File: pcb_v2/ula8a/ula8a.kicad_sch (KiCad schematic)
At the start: 21 parts, among them J1 designador, J2 acc, J3 adder, J4 xor, J5 bitwise, J6 shifter, J7 sx, U1 74LS86, U2 74LS86, U3 74LS86, U4 74LS86, U5 74LS244, U6 74LS86, U7 74LS86

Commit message: roteamento refeito; ainda pendente
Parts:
- removed J2: acc, edge_connector:edge-conector-14, symbol Connector_Generic:Conn_02x14_Top_Bottom
- added C10, C11, C12, C13, C14, C15, C17, C21, C22, C8, C9: 100nF, Capacitor_THT:C_Disc_D5.1mm_W3.2mm_P5.00mm, symbol Device:C
- added D1, D2, D3, D4, D5, D6, D7, D8: 1N4148, Diode_THT:D_DO-35_SOD27_P7.62mm_Horizontal, symbol Diode:1N4148
- added D10: ULA, LED_THT:LED_D5.0mm, symbol Device:LED
- added D11: ~{LOWER}, LED_THT:LED_D5.0mm, symbol Device:LED
- added D12: ~{ULA}, LED_THT:LED_D5.0mm, symbol Device:LED
- added D13: ~{UPPER}, LED_THT:LED_D5.0mm, symbol Device:LED
- added D14: INT, LED_THT:LED_D5.0mm, symbol Device:LED
- added D15: NEG, LED_THT:LED_D5.0mm, symbol Device:LED
- added D16: OVF, LED_THT:LED_D5.0mm, symbol Device:LED
- added D17: CARRY, LED_THT:LED_D5.0mm, symbol Device:LED
- added D18: ZERO, LED_THT:LED_D5.0mm, symbol Device:LED
- added D19: WPSW, LED_THT:LED_D5.0mm, symbol Device:LED
- added D20: WACC, LED_THT:LED_D5.0mm, symbol Device:LED
- added D9: POWER, LED_THT:LED_D5.0mm, symbol Device:LED
- added J7: ula_opp, edge_connector:male-edge-connector-44, symbol Connector_Generic:Conn_02x22_Top_Bottom
- added J8: bus_mgrf_1, Connector_PinHeader_2.54mm:PinHeader_2x08_P2.54mm_Vertical, symbol Connector_Generic:Conn_02x08_Odd_Even
- added J9: bus_mgrf_2, Connector_PinHeader_2.54mm:PinHeader_2x08_P2.54mm_Vertical, symbol Connector_Generic:Conn_02x08_Odd_Even
- added Q1: BC548, Package_TO_SOT_THT:TO-92_Inline, symbol Transistor_BJT:BC548
- added R1, R2: 10K, Resistor_THT:R_Axial_DIN0207_L6.3mm_D2.5mm_P7.62mm_Horizontal, symbol Device:R
- added R10, R11, R12, R13, R14, R15, R16, R17, R18, R19, R20, R9: 1K, Resistor_THT:R_Axial_DIN0207_L6.3mm_D2.5mm_P7.62mm_Horizontal, symbol Device:R
- added U10, U12, U17, U21: 74LS244, Package_DIP:DIP-20_W7.62mm, symbol 74xx:74LS244
- added U11: 74LS86, Package_DIP:DIP-14_W7.62mm, symbol 74xx:74LS86
- added U13, U8: 74LS574, Package_DIP:DIP-20_W7.62mm, symbol 74xx:74LS574
- added U14, U9: 74LS00, Package_DIP:DIP-14_W7.62mm, symbol 74xx:74LS00
- added U15: MC14495P, Package_DIP:DIP-16_W7.62mm, symbol Driver_LED:MC14495P
- added U16: SA39-11EWA, Display_7Segment:Sx39-1xxxxx, symbol Display_Character:SA39-11EWA
- added U22: 74LS04, Package_DIP:DIP-14_W7.62mm, symbol 74xx:74LS04
- C1, C2, C3, C4, C5, C6, C7: footprint (none) -> Capacitor_THT:C_Disc_D5.1mm_W3.2mm_P5.00mm
- J1: footprint edge_connector:edge-connector-44 -> edge_connector:male-edge-connector-44
- J2: renamed from J3; value adder -> ula_opp; footprint edge_connector:edge-connector-44 -> edge_connector:male-edge-connector-44
- J3: renamed from J4; value xor -> ula_opp; footprint edge_connector:edge-connector-44 -> edge_connector:male-edge-connector-44
- J4: renamed from J5; value bitwise -> ula_opp; footprint edge_connector:edge-connector-44 -> edge_connector:male-edge-connector-44
- J5: renamed from J6; value shifter -> ula_opp; footprint edge_connector:edge-connector-44 -> edge_connector:male-edge-connector-44
- J6: renamed from J7; value sx -> ula_opp; footprint edge_connector:edge-connector-44 -> edge_connector:male-edge-connector-44
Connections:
- net carry_in is gone; now on net +5V: J2.23 (Pin_23), J3.23 (Pin_23), J4.23 (Pin_23), J5.23 (Pin_23), J6.23 (Pin_23)
- net clrif is gone; now on net ~{select_sx}: J1.28 (Pin_28)
- net data_out_0 is gone; now on net data_0: U5.18 (O0a)
- net data_out_1 is gone; now on net data_1: U5.16 (O1a)
- net data_out_2 is gone; now on net data_2: U5.14 (O2a)
- net data_out_3 is gone; now on net data_3: U5.12 (O3a)
- net data_out_4 is gone; now on net data_4: U5.9 (O0b)
- net data_out_5 is gone; now on net data_5: U5.7 (O1b)
- net data_out_6 is gone; now on net data_6: U5.5 (O2b)
- net data_out_7 is gone; now on net data_7: U5.3 (O3b)
- net setif is gone; now on net invert_upper_bus: J1.6 (Pin_6)
- net +5V: now also J1.1 (Pin_1), J1.23 (Pin_23), J2.1 (Pin_1), J3.1 (Pin_1), J4.1 (Pin_1), J5.1 (Pin_1), J6.1 (Pin_1), C10.2, C11.2, C12.2, C13.2, C14.2, C15.2, C17.2, C21.2, C22.2, C8.2, C9.2, J7.1 (Pin_1), J7.23 (Pin_23), J8.1 (Pin_1), J8.2 (Pin_2), R9.1, U10.20 (VCC), U11.12, U11.14 (VCC), U11.9, U12.20 (VCC), U13.20 (VCC), U14.1, U14.14 (VCC), U14.2, U15.16 (VCC), U17.20 (VCC), U21.20 (VCC), U22.11, U22.13, U22.14 (VCC), U8.20 (VCC), U9.12, U9.13, U9.14 (VCC); no longer J1.14 (Pin_14), J1.36 (Pin_36), J2.10 (Pin_10), J2.32 (Pin_32), J3.10 (Pin_10), J3.32 (Pin_32), J4.10 (Pin_10), J4.32 (Pin_32), J5.10 (Pin_10), J5.32 (Pin_32), J6.10 (Pin_10), J6.32 (Pin_32)
- net GND: now also J1.22 (Pin_22), J1.44 (Pin_44), J2.22 (Pin_22), J2.44 (Pin_44), J3.22 (Pin_22), J3.44 (Pin_44), J4.22 (Pin_22), J4.44 (Pin_44), J5.22 (Pin_22), J5.44 (Pin_44), J6.22 (Pin_22), J6.44 (Pin_44), C10.1, C11.1, C12.1, C13.1, C14.1, C15.1, C17.1, C21.1, C22.1, C8.1, C9.1, D9.1 (K), J7.22 (Pin_22), J7.44 (Pin_44), J8.15 (Pin_15), J8.16 (Pin_16), Q1.3 (E), R1.2, R10.2, R11.2, R12.2, R13.2, R14.2, R15.2, R16.2, R17.2, R18.2, R19.2, R20.2, U10.10 (GND), U11.7 (GND), U12.10 (GND), U12.13 (I1b), U12.15 (I2b), U12.17 (I3b), U13.1 (OE), U13.10 (GND), U13.6 (D4), U13.7 (D5), U13.8 (D6), U13.9 (D7), U14.7 (GND), U15.7 (~{CLK}), U15.8 (GND), U17.10 (GND), U17.11 (I0b), U17.13 (I1b), U17.15 (I2b), U17.17 (I3b), U21.10 (GND), U21.11 (I0b), U21.13 (I1b), U21.15 (I2b), U21.17 (I3b), U22.7 (GND), U8.1 (OE), U8.10 (GND), U9.7 (GND); no longer J1.15 (Pin_15), J1.37 (Pin_37), J2.11 (Pin_11), J2.33 (Pin_33), J3.11 (Pin_11), J3.33 (Pin_33), J4.11 (Pin_11), J4.33 (Pin_33), J5.11 (Pin_11), J5.33 (Pin_33), J6.11 (Pin_11), J6.33 (Pin_33)
- net invert_lower_bus: now also J1.2 (Pin_2), D11.2 (A); no longer J1.1 (Pin_1)
- net invert_ula_bus: now also J1.5 (Pin_5), D12.2 (A); no longer J1.4 (Pin_4)
- net invert_upper_bus: now also D13.2 (A); no longer J1.5 (Pin_5)
- net lower_bus0: now also J2.2 (Pin_2), J3.2 (Pin_2), J4.2 (Pin_2), J5.2 (Pin_2), J6.2 (Pin_2), J7.2 (Pin_2); no longer J2.1 (Pin_1), J3.1 (Pin_1), J4.1 (Pin_1), J5.1 (Pin_1), J6.1 (Pin_1)
- net lower_bus1: now also J2.3 (Pin_3), J3.3 (Pin_3), J4.3 (Pin_3), J5.3 (Pin_3), J6.3 (Pin_3), J7.3 (Pin_3); no longer J2.2 (Pin_2), J3.2 (Pin_2), J4.2 (Pin_2), J5.2 (Pin_2), J6.2 (Pin_2)
- net lower_bus2: now also J2.4 (Pin_4), J3.4 (Pin_4), J4.4 (Pin_4), J5.4 (Pin_4), J6.4 (Pin_4), J7.4 (Pin_4); no longer J2.3 (Pin_3), J3.3 (Pin_3), J4.3 (Pin_3), J5.3 (Pin_3), J6.3 (Pin_3)
- net lower_bus3: now also J2.5 (Pin_5), J3.5 (Pin_5), J4.5 (Pin_5), J5.5 (Pin_5), J6.5 (Pin_5), J7.5 (Pin_5); no longer J2.4 (Pin_4), J3.4 (Pin_4), J4.4 (Pin_4), J5.4 (Pin_4), J6.4 (Pin_4)
- net lower_bus4: now also J2.6 (Pin_6), J3.6 (Pin_6), J4.6 (Pin_6), J5.6 (Pin_6), J6.6 (Pin_6), J7.6 (Pin_6); no longer J2.5 (Pin_5), J3.5 (Pin_5), J4.5 (Pin_5), J5.5 (Pin_5), J6.5 (Pin_5)
- net lower_bus5: now also J2.7 (Pin_7), J3.7 (Pin_7), J4.7 (Pin_7), J5.7 (Pin_7), J6.7 (Pin_7), J7.7 (Pin_7); no longer J2.6 (Pin_6), J3.6 (Pin_6), J4.6 (Pin_6), J5.6 (Pin_6), J6.6 (Pin_6)
- net lower_bus6: now also J2.8 (Pin_8), J3.8 (Pin_8), J4.8 (Pin_8), J5.8 (Pin_8), J6.8 (Pin_8), J7.8 (Pin_8); no longer J2.7 (Pin_7), J3.7 (Pin_7), J4.7 (Pin_7), J5.7 (Pin_7), J6.7 (Pin_7)
- net lower_bus7: now also J2.9 (Pin_9), J3.9 (Pin_9), J4.9 (Pin_9), J5.9 (Pin_9), J6.9 (Pin_9), J7.9 (Pin_9), U11.1; no longer J2.8 (Pin_8), J3.8 (Pin_8), J4.8 (Pin_8), J5.8 (Pin_8), J6.8 (Pin_8)
- net rd_addr_0: now also J1.19 (Pin_19), J9.8 (Pin_8); no longer J1.20 (Pin_20)
- net rd_addr_1: now also J1.20 (Pin_20), J9.10 (Pin_10); no longer J1.21 (Pin_21)
- net rd_addr_2: now also J1.40 (Pin_40), J9.12 (Pin_12); no longer J1.41 (Pin_41)
- net rd_addr_3: now also J1.41 (Pin_41), J9.14 (Pin_14); no longer J1.42 (Pin_42)
- net rd_addr_4: now also J1.42 (Pin_42), J9.16 (Pin_16); no longer J1.43 (Pin_43)
- net to_acc_0: now also D1.2 (A), U8.2 (D0)
- net to_acc_1: now also D2.2 (A), U8.3 (D1)
- net to_acc_2: now also D3.2 (A), U8.4 (D2)
- net to_acc_3: now also D4.2 (A), U8.5 (D3)
- net to_acc_4: now also D5.2 (A), U8.6 (D4)
- net to_acc_5: now also D6.2 (A), U8.7 (D5)
- net to_acc_6: now also D7.2 (A), U8.8 (D6)
- net to_acc_7: now also D8.2 (A), U11.4, U17.8 (I3a), U8.9 (D7)
- net ula_bus0: now also J2.36 (Pin_36), J3.36 (Pin_36), J4.36 (Pin_36), J5.36 (Pin_36), J6.36 (Pin_36), J7.36 (Pin_36), U10.18 (O0a); no longer J2.37 (Pin_37), J3.37 (Pin_37), J4.37 (Pin_37), J5.37 (Pin_37), J6.37 (Pin_37)
- net ula_bus1: now also J2.37 (Pin_37), J3.37 (Pin_37), J4.37 (Pin_37), J5.37 (Pin_37), J6.37 (Pin_37), J7.37 (Pin_37), U10.16 (O1a); no longer J2.38 (Pin_38), J3.38 (Pin_38), J4.38 (Pin_38), J5.38 (Pin_38), J6.38 (Pin_38)
- net ula_bus2: now also J2.38 (Pin_38), J3.38 (Pin_38), J4.38 (Pin_38), J5.38 (Pin_38), J6.38 (Pin_38), J7.38 (Pin_38), U10.14 (O2a); no longer J2.39 (Pin_39), J3.39 (Pin_39), J4.39 (Pin_39), J5.39 (Pin_39), J6.39 (Pin_39)
- net ula_bus3: now also J2.39 (Pin_39), J3.39 (Pin_39), J4.39 (Pin_39), J5.39 (Pin_39), J6.39 (Pin_39), J7.39 (Pin_39), U10.12 (O3a); no longer J2.40 (Pin_40), J3.40 (Pin_40), J4.40 (Pin_40), J5.40 (Pin_40), J6.40 (Pin_40)
- net ula_bus4: now also J2.40 (Pin_40), J3.40 (Pin_40), J4.40 (Pin_40), J5.40 (Pin_40), J6.40 (Pin_40), J7.40 (Pin_40), U10.9 (O0b); no longer J2.41 (Pin_41), J3.41 (Pin_41), J4.41 (Pin_41), J5.41 (Pin_41), J6.41 (Pin_41)
- net ula_bus5: now also J2.41 (Pin_41), J3.41 (Pin_41), J4.41 (Pin_41), J5.41 (Pin_41), J6.41 (Pin_41), J7.41 (Pin_41), U10.7 (O1b); no longer J2.42 (Pin_42), J3.42 (Pin_42), J4.42 (Pin_42), J5.42 (Pin_42), J6.42 (Pin_42)
- net ula_bus6: now also J2.42 (Pin_42), J3.42 (Pin_42), J4.42 (Pin_42), J5.42 (Pin_42), J6.42 (Pin_42), J7.42 (Pin_42), U10.5 (O2b); no longer J2.43 (Pin_43), J3.43 (Pin_43), J4.43 (Pin_43), J5.43 (Pin_43), J6.43 (Pin_43)
- net ula_bus7: now also J2.43 (Pin_43), J3.43 (Pin_43), J4.43 (Pin_43), J5.43 (Pin_43), J6.43 (Pin_43), J7.43 (Pin_43), U10.3 (O3b); no longer J2.44 (Pin_44), J3.44 (Pin_44), J4.44 (Pin_44), J5.44 (Pin_44), J6.44 (Pin_44)
- net ula_enable: now also J1.33 (Pin_33), D10.2 (A), J9.2 (Pin_2), R2.2, U22.1, U9.2; no longer J1.32 (Pin_32)
- net upper_bus0: now also J2.25 (Pin_25), J3.25 (Pin_25), J4.25 (Pin_25), J5.25 (Pin_25), J6.25 (Pin_25), J7.25 (Pin_25); no longer J2.24 (Pin_24), J3.24 (Pin_24), J4.24 (Pin_24), J5.24 (Pin_24), J6.24 (Pin_24)
- net upper_bus1: now also J2.26 (Pin_26), J3.26 (Pin_26), J4.26 (Pin_26), J5.26 (Pin_26), J6.26 (Pin_26), J7.26 (Pin_26); no longer J2.25 (Pin_25), J3.25 (Pin_25), J4.25 (Pin_25), J5.25 (Pin_25), J6.25 (Pin_25)
- net upper_bus2: now also J2.27 (Pin_27), J3.27 (Pin_27), J4.27 (Pin_27), J5.27 (Pin_27), J6.27 (Pin_27), J7.27 (Pin_27); no longer J2.26 (Pin_26), J3.26 (Pin_26), J4.26 (Pin_26), J5.26 (Pin_26), J6.26 (Pin_26)
- net upper_bus3: now also J2.28 (Pin_28), J3.28 (Pin_28), J4.28 (Pin_28), J5.28 (Pin_28), J6.28 (Pin_28), J7.28 (Pin_28); no longer J2.27 (Pin_27), J3.27 (Pin_27), J4.27 (Pin_27), J5.27 (Pin_27), J6.27 (Pin_27)
- net upper_bus4: now also J2.29 (Pin_29), J3.29 (Pin_29), J4.29 (Pin_29), J5.29 (Pin_29), J6.29 (Pin_29), J7.29 (Pin_29); no longer J2.28 (Pin_28), J3.28 (Pin_28), J4.28 (Pin_28), J5.28 (Pin_28), J6.28 (Pin_28)
- net upper_bus5: now also J2.30 (Pin_30), J3.30 (Pin_30), J4.30 (Pin_30), J5.30 (Pin_30), J6.30 (Pin_30), J7.30 (Pin_30); no longer J2.29 (Pin_29), J3.29 (Pin_29), J4.29 (Pin_29), J5.29 (Pin_29), J6.29 (Pin_29)
- net upper_bus6: now also J2.31 (Pin_31), J3.31 (Pin_31), J4.31 (Pin_31), J5.31 (Pin_31), J6.31 (Pin_31), J7.31 (Pin_31); no longer J2.30 (Pin_30), J3.30 (Pin_30), J4.30 (Pin_30), J5.30 (Pin_30), J6.30 (Pin_30)
- net upper_bus7: now also J2.32 (Pin_32), J3.32 (Pin_32), J4.32 (Pin_32), J5.32 (Pin_32), J6.32 (Pin_32), J7.32 (Pin_32), U11.2; no longer J2.31 (Pin_31), J3.31 (Pin_31), J4.31 (Pin_31), J5.31 (Pin_31), J6.31 (Pin_31)
- net wr_addr_0: now also J1.30 (Pin_30), J9.5 (Pin_5), U15.5 (A); no longer J1.29 (Pin_29)
- net wr_addr_1: now also J1.31 (Pin_31), J9.7 (Pin_7), U15.6 (B); no longer J1.30 (Pin_30)
- net wr_addr_2: now also J1.32 (Pin_32), J9.9 (Pin_9), U15.9 (C); no longer J1.31 (Pin_31)
- net wr_addr_3: now also J9.11 (Pin_11), U15.10 (D)
- net wr_addr_4: now also J9.13 (Pin_13)
- net write_acc: now also D20.2 (A), U22.9, U9.5
- net write_psw: now also D19.2 (A), U14.5, U22.3
- net ~{read_acc}: now also J1.21 (Pin_21); no longer J1.22 (Pin_22)
- net ~{read_psw}: now also J1.43 (Pin_43), U12.1 (OEa), U12.19 (OEb); no longer J1.44 (Pin_44)
- net ~{select_adder}: now also J1.26 (Pin_26), J3.15 (Pin_15), J4.15 (Pin_15), J5.15 (Pin_15), J6.15 (Pin_15), J7.15 (Pin_15); no longer J1.25 (Pin_25)
- net ~{select_bitwise}: now also J1.24 (Pin_24), J2.18 (Pin_18), J3.18 (Pin_18), J4.18 (Pin_18), J5.18 (Pin_18), J6.18 (Pin_18), J7.18 (Pin_18); no longer J1.23 (Pin_23), J4.15 (Pin_15)
- net ~{select_shifter}: now also J1.27 (Pin_27), J2.17 (Pin_17), J3.17 (Pin_17), J4.17 (Pin_17), J5.17 (Pin_17), J6.17 (Pin_17), J7.17 (Pin_17); no longer J1.26 (Pin_26), J5.15 (Pin_15)
- net ~{select_sx}: now also J2.19 (Pin_19), J3.19 (Pin_19), J4.19 (Pin_19), J5.19 (Pin_19), J6.19 (Pin_19), J7.19 (Pin_19); no longer J1.27 (Pin_27), J6.15 (Pin_15)
- net ~{select_xor}: now also J1.25 (Pin_25), J2.16 (Pin_16), J3.16 (Pin_16), J4.16 (Pin_16), J5.16 (Pin_16), J6.16 (Pin_16), J7.16 (Pin_16); no longer J1.24 (Pin_24), J3.15 (Pin_15)
- net at U5.2 (I0a), U6.2: now also U8.19 (Q0)
- net right/mode: now reaches J6.13 (Pin_13)
- net right/mode: now also J1.4 (Pin_4), J2.13 (Pin_13), J3.13 (Pin_13), J4.13 (Pin_13), J5.13 (Pin_13), J7.13 (Pin_13)
- net rotate/value: now reaches J6.14 (Pin_14)
- net rotate/value: now also J1.3 (Pin_3), J2.14 (Pin_14), J3.14 (Pin_14), J4.14 (Pin_14), J5.14 (Pin_14), J7.14 (Pin_14)
- net ~{select_cf}: now reaches J6.20 (Pin_20)
- net ~{select_cf}: now also J1.29 (Pin_29), J2.20 (Pin_20), J3.20 (Pin_20), J4.20 (Pin_20), J5.20 (Pin_20), J7.20 (Pin_20)
- net at U5.13 (I1b), U7.5: now also U8.14 (Q5)
- net at U5.11 (I0b), U7.2: now also U8.15 (Q4)
- net at U5.15 (I2b), U7.10: now also U8.13 (Q6)
- net at U5.17 (I3b), U7.13: now also U8.12 (Q7)
- net at U5.4 (I1a), U6.5: now also U8.18 (Q1)
- net at U5.6 (I2a), U6.10: now also U8.17 (Q2)
- net at U5.8 (I3a), U6.13: now also U8.16 (Q3)
- net carry_out renamed carry_flag_in
- net carry_flag_in: now also J7.35 (Pin_35), U11.5, U17.4 (I1a)
- net data_in_0 renamed data_0
- net data_0: now also J8.14 (Pin_14), U10.2 (I0a), U12.18 (O0a), U21.2 (I0a)
- net data_in_1 renamed data_1
- net data_1: now also J8.13 (Pin_13), U10.4 (I1a), U12.16 (O1a), U21.4 (I1a)
- net data_in_2 renamed data_2
- net data_2: now also J8.11 (Pin_11), U10.6 (I2a), U12.14 (O2a), U21.6 (I2a)
- net data_in_3 renamed data_3
- net data_3: now also J8.9 (Pin_9), U10.8 (I3a), U12.12 (O3a), U21.8 (I3a)
- net data_in_4 renamed data_4
- net data_4: now also J8.7 (Pin_7), U10.11 (I0b), U12.9 (O0b)
- net data_in_5 renamed data_5
- net data_5: now also J8.5 (Pin_5), U10.13 (I1b), U12.7 (O1b)
- net data_in_6 renamed data_6
- net data_6: now also J8.3 (Pin_3), U10.15 (I2b), U12.5 (O2b)
- net data_in_7 renamed data_7
- net data_7: now also J8.4 (Pin_4), U10.17 (I3b), U12.3 (O3b)
- removed net right/set: J1.3 (Pin_3), J5.16 (Pin_16), J6.16 (Pin_16)
- removed net rotate/clear: J1.2 (Pin_2), J5.17 (Pin_17), J6.17 (Pin_17)
- net write_clock renamed write_enable
- net write_enable: now also J9.15 (Pin_15)
- new net: D16.1 (K), R16.1
- new net: D1.1 (K), D2.1 (K), D3.1 (K), D4.1 (K), D5.1 (K), D6.1 (K), D7.1 (K), D8.1 (K), R1.1, U22.5
- new net: D18.1 (K), R18.1
- new net: U14.10, U9.3, U9.9
- new net: U17.1 (OEa), U17.19 (OEb), U22.2
- new net: D10.1 (K), R10.1
- new net: U11.10, U11.3
- new net: U10.1 (OEa), U10.19 (OEb), U22.8
- new net: U9.10, U9.6
- new net: U14.6, U14.9
- new net: U21.1 (OEa), U21.19 (OEb), U22.4
- new net: U13.5 (D3), U17.12 (O3a), U21.12 (O3a)
- new net: U13.4 (D2), U17.14 (O2a), U21.14 (O2a)
- new net: U13.3 (D1), U17.16 (O1a), U21.16 (O1a)
- new net: U13.2 (D0), U17.18 (O0a), U21.18 (O0a)
- new net: Q1.2 (B), R2.1
- new net: U11.6, U14.13
- new net: U15.3 (g), U16.1 (G)
- new net: U15.12 (a), U16.10 (A)
- new net: U15.2 (f), U16.2 (F)
- new net: Q1.1 (C), U16.3 (CA), U16.8 (CA)
- new net: U15.1 (e), U16.4 (E)
- new net: U15.15 (d), U16.5 (D)
- new net: U15.14 (c), U16.7 (C)
- new net: U15.13 (b), U16.9 (B)
- new net: U11.13, U14.11
- new net: U11.8, U14.12
- new net: D15.1 (K), R15.1
- new net: D19.1 (K), R19.1
- new net: D12.1 (K), R12.1
- new net: D17.1 (K), R17.1
- new net: D9.2 (A), R9.2
- new net: D13.1 (K), R13.1
- new net: D14.1 (K), R14.1
- new net: D11.1 (K), R11.1
- new net: D20.1 (K), R20.1
- new net carry_flag_out: D17.2 (A), J2.24 (Pin_24), J3.24 (Pin_24), J4.24 (Pin_24), J5.24 (Pin_24), J6.24 (Pin_24), J7.24 (Pin_24), J8.8 (Pin_8), U12.4 (I1a), U13.18 (Q1)
- new net clock: J9.4 (Pin_4), U14.4, U9.1, U9.4
- new net int_mask_in: D14.2 (A), J9.1 (Pin_1), U12.11 (I0b)
- new net load_ula_acc: U8.11 (Cp), U9.8
- new net load_ula_psw: U13.11 (Cp), U14.8
- new net negative_flag_out: D15.2 (A), J8.12 (Pin_12), U12.8 (I3a), U13.16 (Q3)
- new net overflow_flag_in: U11.11, U17.6 (I2a)
- new net overflow_flag_out: D16.2 (A), J8.10 (Pin_10), U12.6 (I2a), U13.17 (Q2)
- new net zero_flag_in: U17.2 (I0a), U22.6
- new net zero_flag_out: D18.2 (A), J8.6 (Pin_6), U12.2 (I0a), U13.19 (Q0)
- no-connect marks 79 -> 70
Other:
- moved on the sheet: C1, C2, C3, C4, C5, C6, C7, U1A, U1B, U1C, U1D, U1E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

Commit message: concluidas as modificações de layout na pcb
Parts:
- U16: footprint Display_7Segment:Sx39-1xxxxx -> 7segdisplay:1-digit-13mm
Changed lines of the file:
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@@
 			)
 		)
-		(property "Footprint" "Display_7Segment:Sx39-1xxxxx"
+		(property "Footprint" "7segdisplay:1-digit-13mm"
 			(at 123.19 262.89 0)
 			(effects

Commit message: .
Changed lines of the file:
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@@
 	)
 	(global_label "rd_addr_0"
-		(shape input)
+		(shape output)
 		(at 43.18 172.72 0)
 		(fields_autoplaced yes)
@@
 		)
 		(property "Intersheetrefs" "${INTERSHEET_REFS}"
-			(at 54.9064 172.6406 0)
+			(at 55.4783 172.72 0)
 			(effects
 				(font
@@
 	)
 	(global_label "ula_enable"
-		(shape input)
+		(shape output)
 		(at 43.18 165.1 0)
 		(fields_autoplaced yes)
@@
 	)
 	(global_label "wr_addr_0"
-		(shape input)
+		(shape output)
 		(at 30.48 170.18 180)
 		(fields_autoplaced yes)
@@
 		)
 		(property "Intersheetrefs" "${INTERSHEET_REFS}"
-			(at 18.5721 170.1006 0)
+			(at 18.0002 170.18 0)
 			(effects
 				(font
@@
 	)
 	(global_label "wr_addr_2"
-		(shape input)
+		(shape output)
 		(at 30.48 175.26 180)
 		(fields_autoplaced yes)
@@
 		)
 		(property "Intersheetrefs" "${INTERSHEET_REFS}"
-			(at 18.5721 175.1806 0)
+			(at 18.0002 175.26 0)
 			(effects
 				(font
@@
 	)
 	(global_label "wr_addr_1"
-		(shape input)
+		(shape output)
 		(at 30.48 172.72 180)
 		(fields_autoplaced yes)
@@
 		)
 		(property "Intersheetrefs" "${INTERSHEET_REFS}"
-			(at 18.5721 172.6406 0)
+			(at 18.0002 172.72 0)
 			(effects
 				(font
@@
 	)
 	(global_label "int_mask_in"
-		(shape input)
+		(shape output)
 		(at 30.48 165.1 180)
 		(fields_autoplaced yes)
@@
 	)
 	(global_label "rd_addr_2"
-		(shape input)
+		(shape output)
 		(at 43.18 177.8 0)
 		(fields_autoplaced yes)
@@
 		)
 		(property "Intersheetrefs" "${INTERSHEET_REFS}"
-			(at 54.9064 177.7206 0)
+			(at 55.4783 177.8 0)
 			(effects
 				(font
@@
 	)
 	(global_label "clock"
-		(shape input)
+		(shape output)
 		(at 43.18 167.64 0)
 		(fields_autoplaced yes)
@@
 	)
 	(global_label "wr_addr_4"
-		(shape input)
+		(shape output)
 		(at 30.48 180.34 180)
 		(fields_autoplaced yes)
@@
 		)
 		(property "Intersheetrefs" "${INTERSHEET_REFS}"
-			(at 18.5721 180.2606 0)
+			(at 18.0002 180.34 0)
 			(effects
 				(font
@@
 	)
 	(global_label "rd_addr_1"
-		(shape input)
+		(shape output)
 		(at 43.18 175.26 0)
 		(fields_autoplaced yes)
@@
 		)
 		(property "Intersheetrefs" "${INTERSHEET_REFS}"
-			(at 54.9064 175.1806 0)
+			(at 55.4783 175.26 0)
 			(effects
 				(font
@@
 	)
 	(global_label "wr_addr_3"
-		(shape input)
+		(shape output)
 		(at 30.48 177.8 180)
 		(fields_autoplaced yes)
@@
 		)
 		(property "Intersheetrefs" "${INTERSHEET_REFS}"
-			(at 18.5721 177.7206 0)
+			(at 18.0002 177.8 0)
 			(effects
 				(font
@@
 	)
 	(global_label "rd_addr_3"
-		(shape input)
+		(shape output)
 		(at 43.18 180.34 0)
 		(fields_autoplaced yes)
@@
 		)
 		(property "Intersheetrefs" "${INTERSHEET_REFS}"
-			(at 54.9064 180.2606 0)
+			(at 55.4783 180.34 0)
 			(effects
 				(font
@@
 	)
 	(global_label "rd_addr_4"
-		(shape input)
+		(shape output)
 		(at 43.18 182.88 0)
 		(fields_autoplaced yes)
@@
 		)
 		(property "Intersheetrefs" "${INTERSHEET_REFS}"
-			(at 54.9064 182.8006 0)
+			(at 55.4783 182.88 0)
 			(effects
 				(font

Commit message: concluído o layout da pcb
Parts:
- D11: value ~{LOWER} -> LOWER
- D12: value ~{ULA} -> ULA
- D13: value ~{UPPER} -> UPPER
- J2, J3, J4, J5, J6, J7: value ula_opp -> operador
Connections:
- net invert_upper_bus: now also U6.10, U6.13, U6.2, U6.5, U7.10; no longer U6.1, U6.12, U6.4, U6.9, U7.9
- net upper_bus0: now also U6.6; no longer U6.3
- net upper_bus1: now also U6.3; no longer U6.6
- net at U5.2 (I0a), U8.19 (Q0): now also U6.1; no longer U6.2
- net at U5.15 (I2b), U8.13 (Q6): now also U7.9; no longer U7.10
- net at U5.4 (I1a), U8.18 (Q1): now also U6.4; no longer U6.5
- net at U5.6 (I2a), U8.17 (Q2): now also U6.9; no longer U6.10
- net at U5.8 (I3a), U8.16 (Q3): now also U6.12; no longer U6.13
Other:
- moved on the sheet: U4A, U4B, U4C, U4D, U6A, U6B, U6C, U6D, U7C

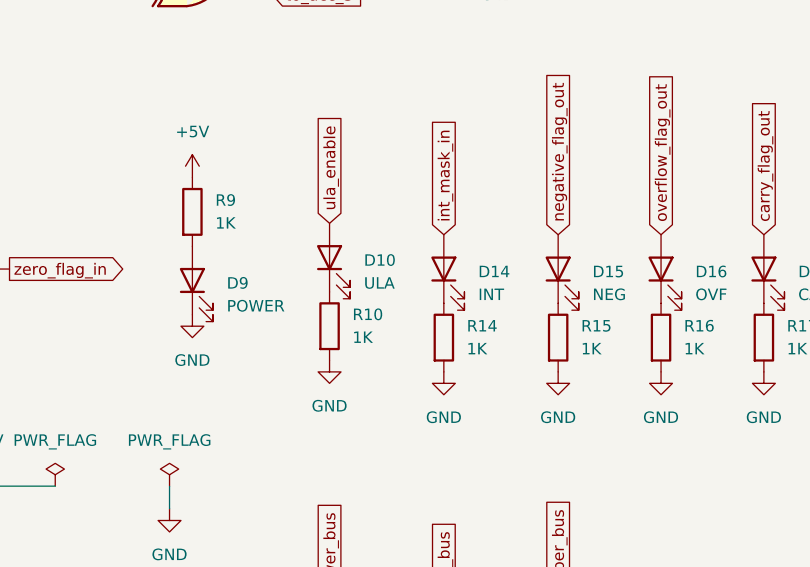
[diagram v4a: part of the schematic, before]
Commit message: inversão na posição dos conectores, para coincidir com o sysbus
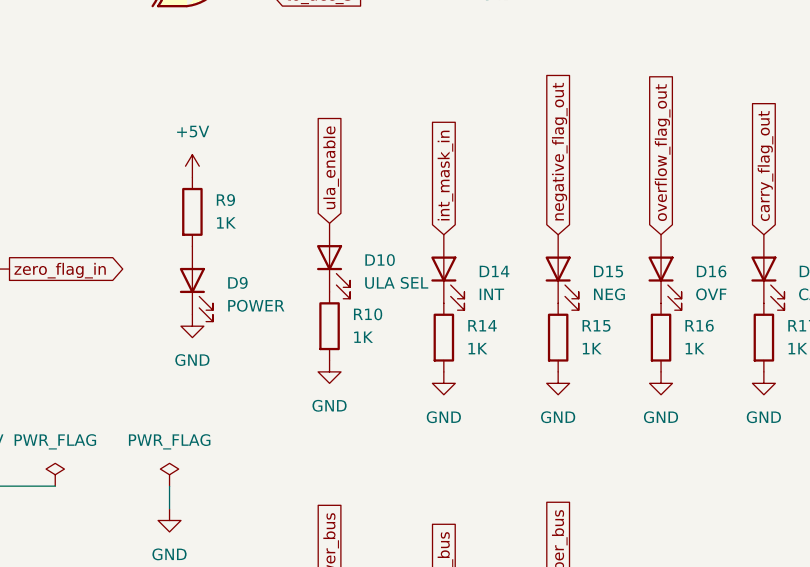
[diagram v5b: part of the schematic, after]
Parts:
- D10: value ULA -> ULA SEL
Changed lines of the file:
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@@
 			)
 		)
-		(property "Value" "ULA"
+		(property "Value" "ULA SEL"
 			(at 156.21 183.1974 90)
 			(effects

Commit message: atualização do conector flat
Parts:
- J8, J9: footprint Connector_PinHeader_2.54mm:PinHeader_2x08_P2.54mm_Vertical -> edge_connector:conector 02x08
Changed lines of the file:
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@@
 			)
 		)
-		(property "Footprint" "Connector_PinHeader_2.54mm:PinHeader_2x08_P2.54mm_Vertical"
+		(property "Footprint" "edge_connector:conector 02x08"
 			(at 35.56 205.74 0)
 			(effects
@@
 			)
 		)
-		(property "Footprint" "Connector_PinHeader_2.54mm:PinHeader_2x08_P2.54mm_Vertical"
+		(property "Footprint" "edge_connector:conector 02x08"
 			(at 35.56 172.72 0)
 			(effects
